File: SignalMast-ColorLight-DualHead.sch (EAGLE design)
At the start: 8 parts

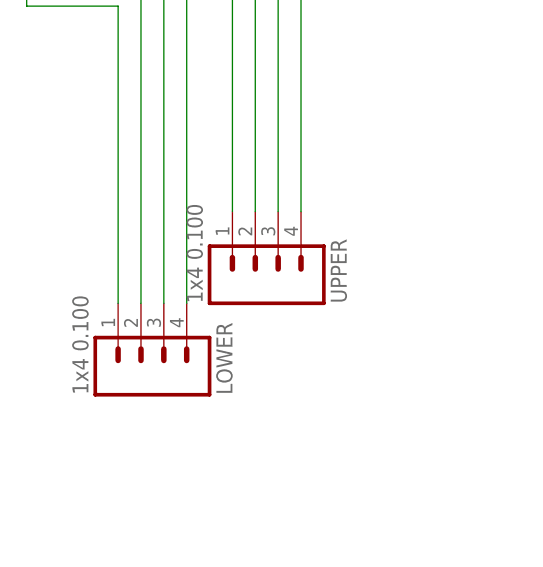
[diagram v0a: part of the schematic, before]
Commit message: normalized values
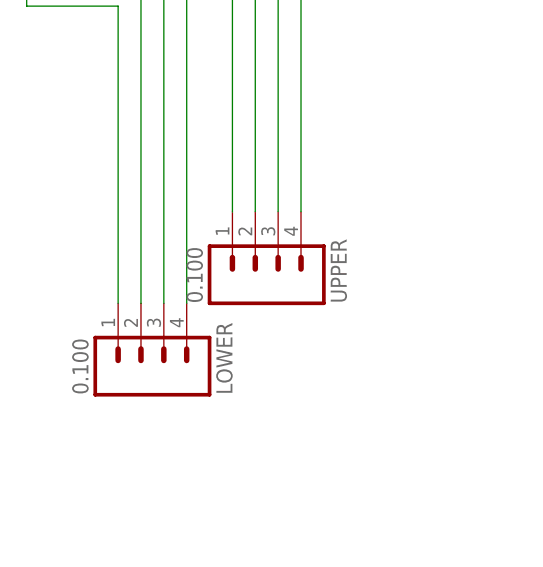
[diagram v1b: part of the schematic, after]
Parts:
- LOWER, UPPER: value 1x4 0.100 -> 0.100
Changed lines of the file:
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@@
 <parts>
 <part name="FRAME1" library="SPCoast" deviceset="DOC-FRAME-LETTER" device="" value="John Plocher"/>
-<part name="UPPER" library="SPCoast" deviceset="CONNECTOR-M04" device="LOCK" value="1x4 0.100"/>
-<part name="LOWER" library="SPCoast" deviceset="CONNECTOR-M04" device="LOCK" value="1x4 0.100"/>
+<part name="UPPER" library="SPCoast" deviceset="CONNECTOR-M04" device="LOCK" value="0.100"/>
+<part name="LOWER" library="SPCoast" deviceset="CONNECTOR-M04" device="LOCK" value="0.100"/>
 <part name="LED1" library="SPCoast" deviceset="LED*" device="0603-LED" value="R">
 <attribute name="OPL" value="19-217-R6C-AL1M2VY-3T"/>
